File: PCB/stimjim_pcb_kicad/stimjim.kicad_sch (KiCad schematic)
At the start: 163 parts, among them J1 Conn_02x08_Odd_Even, J2 Conn_Coaxial, J3 Conn_Coaxial, J6 Screw_Terminal_01x02, J7 Conn_Coaxial, J8 Screw_Terminal_01x02, J9 Conn_Coaxial, SW1 SW_Push, U1 Teensy3.5, U10 AMP03, U11 INA826, U12 DG509ACWE, U13 CC3-0512DF-E, U14 ISO7760, U15 ISO7741, U16 L78L05_SO8, U17 AD5752, U18 AD7321, U19 AD1582, U2 CC3-0512DF-E, U20 OPA197, U21 AMP03, U22 INA826, U23 DG509ACWE, U3 ISO7760, U4 ISO7741, U5 L78L05_SO8, U6 AD5752, U7 AD7321, U8 AD1582, U9 OPA197

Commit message: Merged in nc-move-channels-to-subsheet (pull request #4)
Move channel schematic to subsheet, make two instances of it. Fix the ERC and DRC errors I made.
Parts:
- removed C1, C11, C13, C14, C16, C17, C18, C19, C2, C20, C21, C22, C23, C24, C25, C26, C27, C31, C32, C34, C35, C38, C39, C41, C42, C43, C44, C45, C46, C47, C48, C49, C50, C6, C7, C9: 0.1uF, Capacitor_SMD:C_0603_1608Metric, symbol Device:C_Small
- removed C10, C12, C15, C33, C36, C37, C40, C51, C52, C8: 1uF, Capacitor_SMD:C_0603_1608Metric, symbol Device:C_Small
- removed C28, C29, C3, C30, C4, C5: 10uF, Capacitor_SMD:C_1206_3216Metric_Pad1.42x1.75mm_HandSolder, symbol Device:C_Small
- removed C53, C54: 2.2nF, Capacitor_SMD:C_1210_3225Metric_Pad1.42x2.65mm_HandSolder, symbol Device:C_Small
- removed J6, J8: Screw_Terminal_01x02, microstim:1-2834016-2 _TERM_BLK_2P_SIDE_ENT_2.54MM_PCB, symbol Connector:Screw_Terminal_01x02
- removed J7, J9: Conn_Coaxial, microstim:731375003, symbol Connector:Conn_Coaxial
- removed R1, R17, R18, R8: 10k, Resistor_SMD:R_0603_1608Metric, symbol Device:R_US
- removed R10, R3: 5k, Resistor_SMD:R_0603_1608Metric, symbol Device:R_US
- removed R11, R2, R4, R9: 3k, Resistor_SMD:R_0603_1608Metric, symbol Device:R_US
- removed R12, R5: 100, Resistor_SMD:R_0603_1608Metric, symbol Device:R_US
- removed R13, R6: 1.8k, Resistor_SMD:R_0603_1608Metric, symbol Device:R_US
- removed R14, R7: 1k, Resistor_SMD:R_0603_1608Metric, symbol Device:R_US
- removed R19, R20: 1M, Resistor_SMD:R_1210_3225Metric_Pad1.42x2.65mm_HandSolder, symbol Device:R_Small_US
- removed TP15, TP16, TP17, TP18, TP19, TP20, TP21, TP22: TestPoint, TestPoint:TestPoint_THTPad_1.0x1.0mm_Drill0.5mm, symbol Connector:TestPoint
- removed TP23, TP24, TP25, TP26, TP27, TP28, TP29, TP30, TP31, TP32, TP33, TP34, TP37, TP38, TP39, TP40, TP41, TP42, TP43, TP44, TP45, TP48, TP49, TP50, TP51, TP52: TestPoint, TestPoint:TestPoint_THTPad_D1.0mm_Drill0.5mm, symbol Connector:TestPoint
- removed U10, U21: AMP03, Package_SO:SOIC-8_3.9x4.9mm_P1.27mm, symbol stimjimlib:AMP03
- removed U11, U22: INA826, Package_SO:SOIC-8_3.9x4.9mm_P1.27mm, symbol stimjimlib:INA826
- removed U12, U23: DG509ACWE, 21-0042B_16, symbol stimjimlib:DG509ACWE
- removed U13, U2: CC3-0512DF-E, microstim:CC3-0512DF-E, symbol stimjimlib:CC3-0512DF-E
- removed U14, U3: ISO7760, Package_SO:SOIC-16W_7.5x10.3mm_P1.27mm, symbol stimjimlib:ISO7760
- removed U15, U4: ISO7741, Package_SO:SOIC-16W_7.5x10.3mm_P1.27mm, symbol stimjimlib:ISO7741
- removed U16, U5: L78L05_SO8, Package_SO:SOIC-8_3.9x4.9mm_P1.27mm, symbol Regulator_Linear:L78L05_SO8
- removed U17, U6: AD5752, Package_SO:TSSOP-24_4.4x7.8mm_P0.65mm, symbol stimjimlib:AD5752
- removed U18, U7: AD7321, Package_SO:TSSOP-14_4.4x5mm_P0.65mm, symbol stimjimlib:AD7321
- removed U19, U8: AD1582, Package_TO_SOT_SMD:SOT-23, symbol stimjimlib:AD1582
- removed U20, U9: OPA197, Package_SO:SOIC-8_3.9x4.9mm_P1.27mm, symbol stimjimlib:OPA197
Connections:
- no-connect marks 63 -> 49
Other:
- added sheet channel_0 (channel.kicad_sch)
- added sheet channel_1 (channel.kicad_sch)
- note removed: "Ground coupling"
- note removed: "Max current output (0ohm load) is (+/-10V)/3k = +- 3.33mA. Current resolution is 20V/2^16/3k = 0.1uA Max voltage output (infinite load) is 40/43*14.8V = +/-13.76V"
- note removed: "OE0 OE1 Output 0 0 VOLTAGE 1 0 CURRENT 0 1 High-Z 1 1 GND"
- note removed: "Stim channel 0"
- note removed: "Stim channel 1"
- note removed: "gain is Rsense*(1+49.4k/Rg) = 100*(1+49.4k/1.8k) = 2.87 mV/uA Voltage output range is thus +-3333*0.00287 = +-9.57V output needs to be within +-10V current sensing resolution is 10000 mV / 2^12 / (2.87mV/uA) = 0.85uA"
- moved on the sheet: H1, H2, H3, H4, J1, TP1, TP10, TP11, TP12, TP13, TP14, TP2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

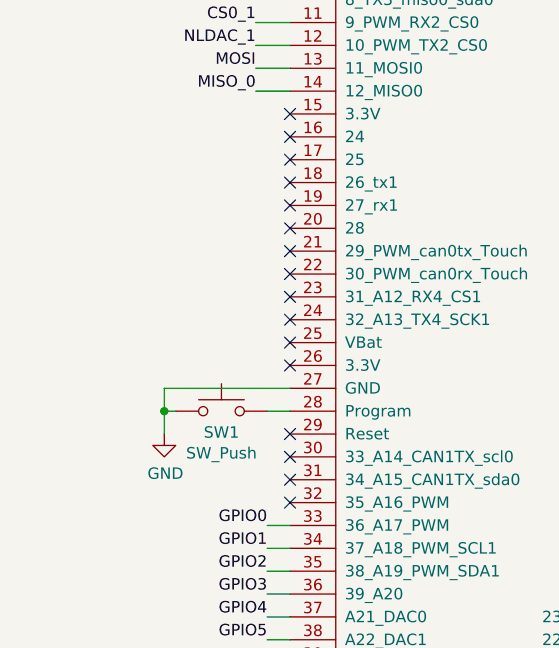
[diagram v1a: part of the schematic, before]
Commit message: Minor edits to PCB
- Expose access to program button at test point that can be soldered to
pin 28 using a wire
- Increase tolerance on tight digital trace routing
- Add keepout area to top copper at the point where the shield on the
isolated DC power supply comes in close proximity to isolated ground.
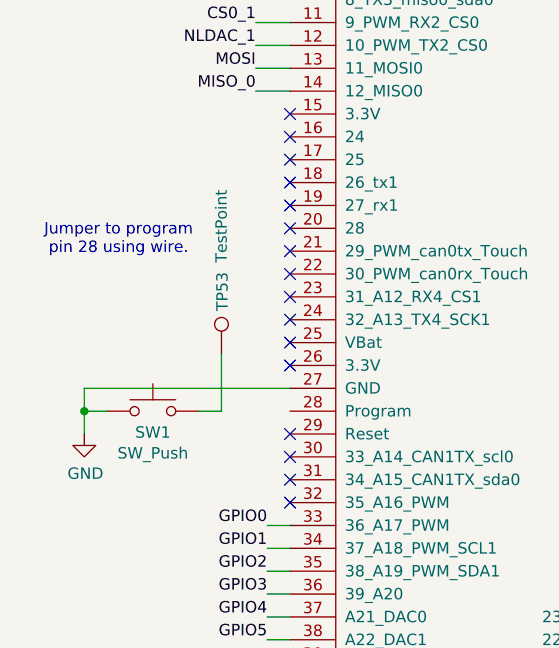
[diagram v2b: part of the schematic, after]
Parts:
- added TP53: TestPoint, TestPoint:TestPoint_THTPad_D2.0mm_Drill1.0mm, symbol Connector:TestPoint
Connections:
- net at U1.28 (Program): no longer SW1.2
- new net: SW1.2, TP53.1
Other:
- note added: "Jumper to program pin 28 using wire."
- moved on the sheet: SW1

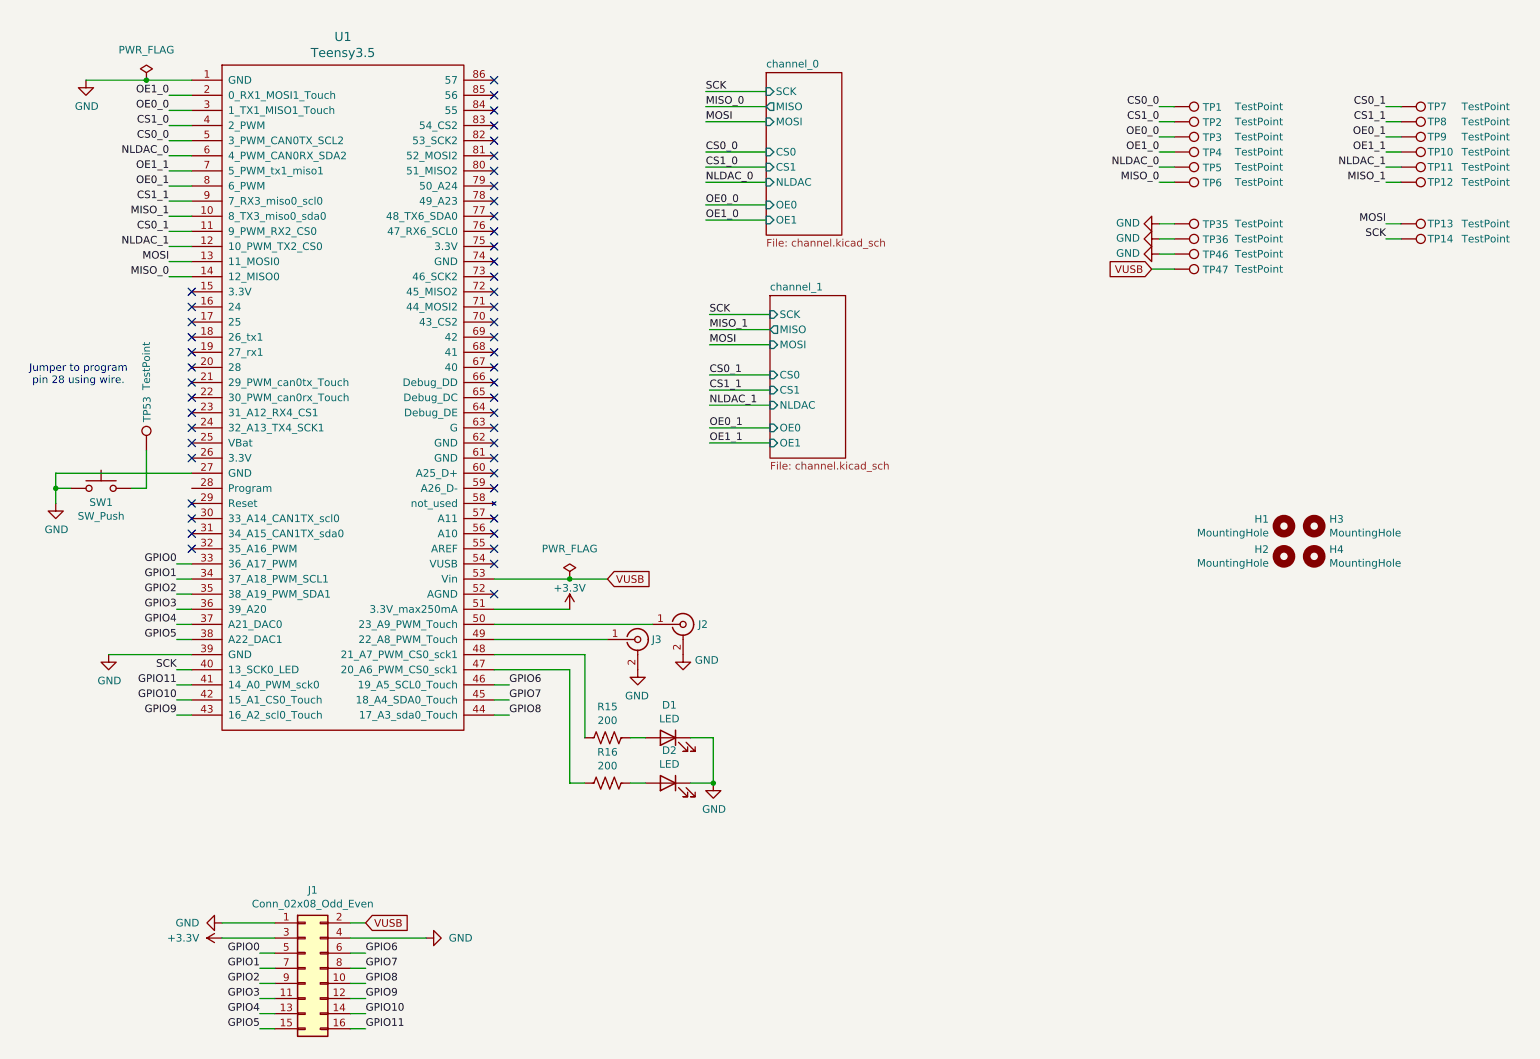
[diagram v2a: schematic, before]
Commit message: Replace teensy with RP235xB
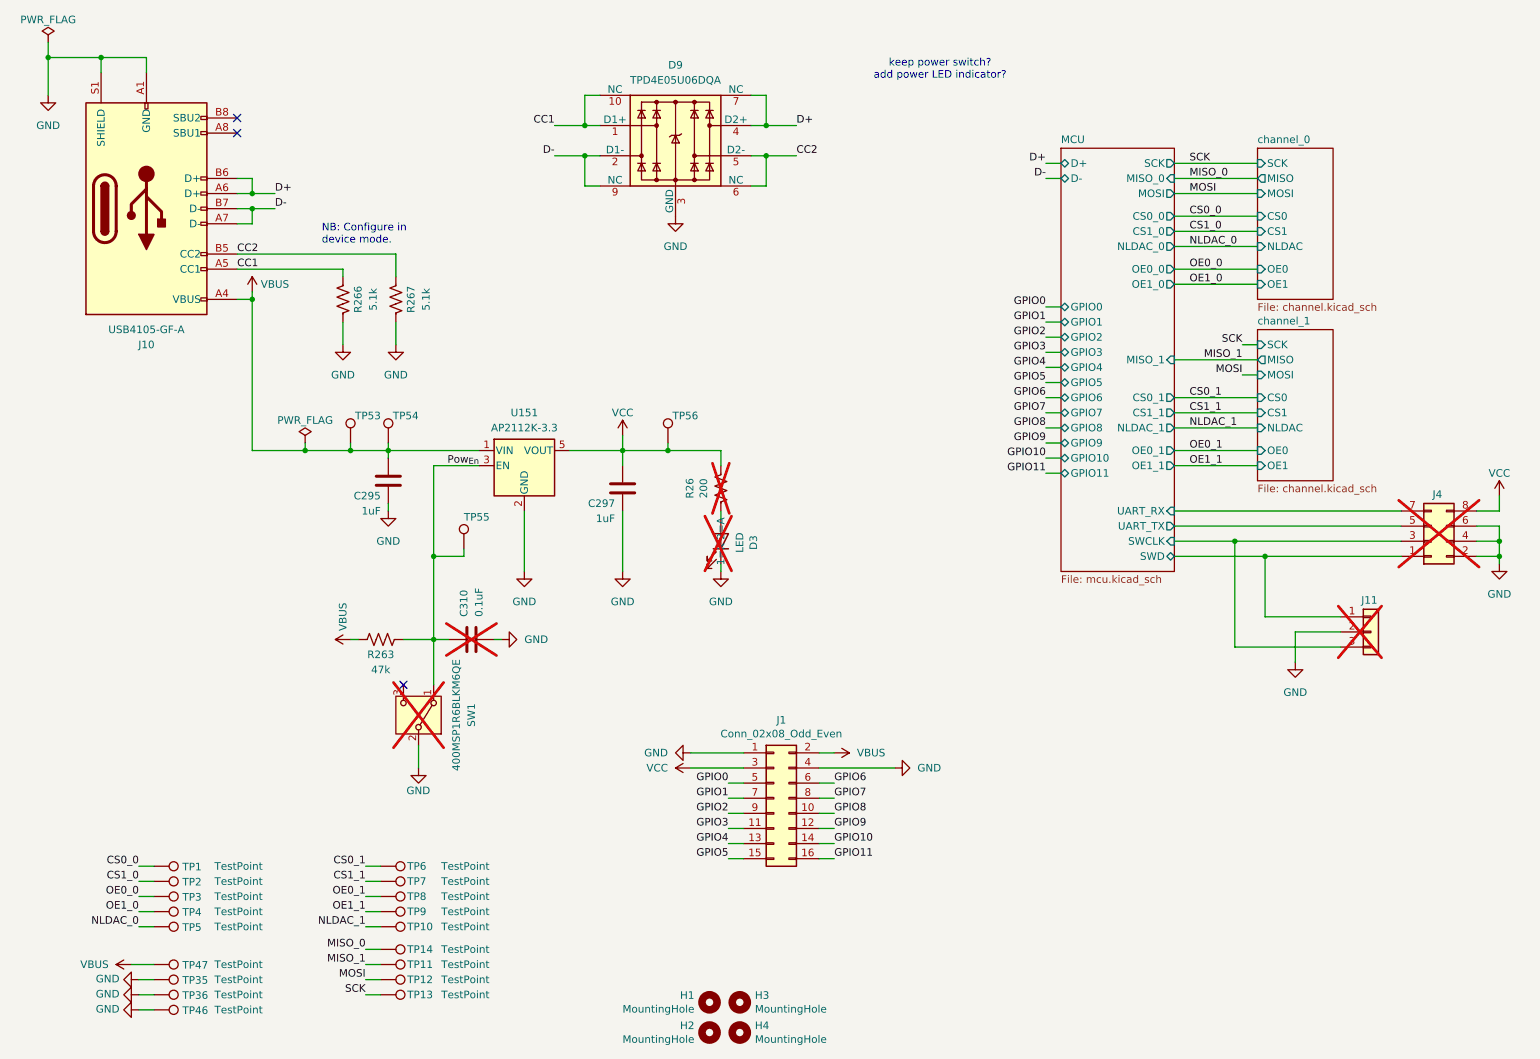
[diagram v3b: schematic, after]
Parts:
- removed D1, D2: LED, microstim:LED_D5.0mm_Horizontal_O1.27mm_Z3.0mm_pinSwapped, symbol Device:LED
- removed J2, J3: Conn_Coaxial, microstim:731375003, symbol Connector:Conn_Coaxial
- removed R15, R16: 200, Resistor_SMD:R_0603_1608Metric, symbol Device:R_US
- removed SW1: SW_Push, microstim:EVQ-PF303K, symbol Switch:SW_Push
- removed TP6: TestPoint, TestPoint:TestPoint_THTPad_D1.0mm_Drill0.5mm, symbol Connector:TestPoint
- removed U1: Teensy3.5, microstim:Teensy35_36_noInternalPins, symbol teensy:Teensy3.5
- added C295, C297: 1uF, Capacitor_SMD:C_0603_1608Metric, symbol Device:C
- added C310: 0.1uF, Capacitor_SMD:C_0402_1005Metric, symbol Device:C
- added D3: LED, microstim:LED_D5.0mm_Horizontal_O1.27mm_Z3.0mm_pinSwapped, symbol Device:LED
- added D9: TPD4E05U06DQA, Package_SON:USON-10_2.5x1.0mm_P0.5mm, symbol Power_Protection:TPD4E05U06DQA
- added J10: USB4105-GF-A, Connector_USB:USB_C_Receptacle_GCT_USB4105-xx-A_16P_TopMnt_Horizontal, symbol Connector:USB_C_Receptacle_USB2.0_16P
- added J11: BM03B-SRSS-TB, Connector_JST:JST_SH_BM03B-SRSS-TB_1x03-1MP_P1.00mm_Vertical, symbol Connector_Generic:Conn_01x03
- added J4: 10129383-910002ALF, Connector_PinHeader_2.54mm:PinHeader_2x04_P2.54mm_Vertical_SMD, symbol Connector_Generic:Conn_02x04_Odd_Even
- added R26: 200, Resistor_SMD:R_0603_1608Metric, symbol Device:R_US
- added R263: 47k, Resistor_SMD:R_0402_1005Metric, symbol Device:R_US
- added R266, R267: 5.1k, Resistor_SMD:R_0402_1005Metric, symbol Device:R_US
- added SW1: 400MSP1R6BLKM6QE, Button_Switch_THT:SW_Push_2P2T_Vertical_E-Switch_800UDP8P1A1M6, symbol Switch:SW_SPDT
- added TP14: TestPoint, TestPoint:TestPoint_THTPad_D1.0mm_Drill0.5mm, symbol Connector:TestPoint
- added TP54, TP55: GND, TestPoint:TestPoint_Pad_D2.0mm, symbol Connector:TestPoint
- added TP56: VCC, TestPoint:TestPoint_Pad_D2.0mm, symbol Connector:TestPoint
- added U151: AP2112K-3.3, Package_TO_SOT_SMD:SOT-23-5, symbol Regulator_Linear:AP2112K-3.3
- H1, H2, H3, H4, TP1, TP2, TP3, TP35, TP36, TP4, TP46, TP47, TP5: now left out of the parts list
- TP10: renamed from TP11; now left out of the parts list
- TP11: renamed from TP12; now left out of the parts list
- TP12: renamed from TP13; now left out of the parts list
- TP13: renamed from TP14; now left out of the parts list
- TP53: value TestPoint -> GND; footprint TestPoint:TestPoint_THTPad_D2.0mm_Drill1.0mm -> TestPoint:TestPoint_Pad_D2.0mm; now left out of the parts list
- TP6: renamed from TP7; now left out of the parts list
- TP7: renamed from TP8; now left out of the parts list
- TP8: renamed from TP9; now left out of the parts list
- TP9: renamed from TP10; now left out of the parts list
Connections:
- net VUSB is gone; now on net VBUS: J1.2 (Pin_2), TP47.1
- net GND: now also C295.2, C297.2, C310.2, D3.1 (K), D9.3 (GND), D9.8 (GND), J10.A1 (GND), J10.A12 (GND), J10.B1 (GND), J10.B12 (GND), J10.S1 (SHIELD), J11.2 (Pin_2), J4.2 (Pin_2), J4.4 (Pin_4), J4.6 (Pin_6), R266.2, R267.2, SW1.2 (B), U151.2 (GND)
- net MISO_0: now also TP14.1
- net VBUS: now reaches TP53.1
- net VBUS: now also C295.1, J10.A4 (VBUS), J10.A9 (VBUS), J10.B4 (VBUS), J10.B9 (VBUS), R263.1, TP54.1, U151.1 (VIN)
- net +3.3V renamed VCC
- net VCC: now also C297.1, J4.8 (Pin_8), R26.1, TP56.1, U151.5 (VOUT)
- new net: D3.2 (A), R26.2
- new net CC1: D9.1 (D1+), D9.10 (NC), J10.A5 (CC1), R266.1
- new net CC2: D9.5 (D2-), D9.6 (NC), J10.B5 (CC2), R267.1
- new net D+: D9.4 (D2+), D9.7 (NC), J10.A6 (D+), J10.B6 (D+)
- new net D-: D9.2 (D1-), D9.9 (NC), J10.A7 (D-), J10.B7 (D-)
- new net MCU/SWCLK: J11.3 (Pin_3), J4.3 (Pin_3)
- new net MCU/SWD: J11.1 (Pin_1), J4.1 (Pin_1)
- new net MCU/UART_RX: J4.7 (Pin_7)
- new net MCU/UART_TX: J4.5 (Pin_5)
- new net Pow_{En}: C310.1, R263.2, SW1.1 (A), TP55.1, U151.3 (EN)
- no-connect marks 49 -> 3
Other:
- added sheet MCU (mcu.kicad_sch)
- note added: "NB: Configure in device mode."
- note added: "keep power switch? add power LED indicator?"
- note removed: "Jumper to program pin 28 using wire."
- moved on the sheet: H1, H2, H3, H4, J1, TP1, TP10, TP11, TP12, TP13, TP2, TP3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
